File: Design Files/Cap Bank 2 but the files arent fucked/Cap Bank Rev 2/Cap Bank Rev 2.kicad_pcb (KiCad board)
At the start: 2 copper layers, 54 x 85.6 mm, 23 parts, among them J1 Conn_01x02, Q1 2N3904, Q2 2N3904, Q3 2N3904, Q4 2N3904

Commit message: updated again!!!
ship it!
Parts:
- removed C2, C4, C6, C8: C_Polarized, Library:smallcap
- added ?: , , F.Cu at (150.0, 111.5)
- added ?: , , F.Cu at (178.6, 127.5)
- added ?: , , F.Cu at (150.0, 88.5)
- added ?: , , F.Cu at (178.6, 72.5)
- added J2: Conn_01x02, Connector_AMASS:AMASS_XT30U-F_1x02_P5.0mm_Vertical, F.Cu at (131.0, 103.2)
- C1, C5: footprint Library:bigcap2pos -> Library:bigcap
- C3, C7: footprint Library:bigcap2neg -> Library:bigcap
- J1: footprint Library:xt30 -> Connector_AMASS:AMASS_XT30U-M_1x02_P5.0mm_Vertical
- moved REF** 23.0 mm to (150.0, 111.5)
- moved REF** 23.0 mm to (150.0, 88.5)
- moved J1 7.08 mm to (131.0, 96.8), turned to 180 degrees
- moved C1 5.21 mm to (137.5, 121.5)
- moved C3 5.21 mm to (162.5, 121.5)
- moved C5 5.21 mm to (162.5, 78.5)
- moved C7 5.21 mm to (137.5, 78.5)
- moved Q1 2.00 mm to (140.0, 103.0)
- moved Q2 2.00 mm to (160.0, 103.0)
- moved Q3 2.00 mm to (160.0, 97.0)
- moved Q4 2.00 mm to (140.0, 97.0)
- moved R1 2.00 mm to (136.0, 101.2)
- moved R2 2.00 mm to (144.0, 101.2)
- moved R3 2.00 mm to (156.0, 101.2)
- moved R4 2.00 mm to (164.0, 101.2)
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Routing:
- net /V_IN: track 4.40 -> 0.40 mm
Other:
- board size 54 x 85.6 mm -> 62 x 67 mm

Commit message: new bjt
who dis
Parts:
- added D1: LED, LED_THT:LED_D3.0mm_Clear, F.Cu at (128.6, 84.4)
- added R9: 1000, Resistor_THT:R_Axial_DIN0207_L6.3mm_D2.5mm_P7.62mm_Horizontal, F.Cu at (123.0, 92.0)
- Q1, Q2, Q3, Q4: value 2N3904 -> TIP31; footprint Library:2n3904 -> Library:tip31
- moved ? 57.3 mm to (121.4, 127.5)
- moved ? 57.3 mm to (121.4, 72.5)
- moved R6 11.1 mm to (165.4, 92.9), turned to 180 degrees
- moved R2 10.7 mm to (134.8, 106.7), turned to 0 degrees
- moved R8 9.96 mm to (144.1, 92.9), turned to 180 degrees
- moved R4 9.92 mm to (155.7, 106.7), turned to 0 degrees
- moved Q4 8.97 mm to (138.9, 88.1), turned to 180 degrees
- moved Q3 8.82 mm to (160.4, 88.2), turned to 180 degrees
- moved Q1 8.63 mm to (139.8, 111.6), turned to 0 degrees
- moved Q2 8.58 mm to (160.7, 111.5), turned to 0 degrees
- moved R5 4.70 mm to (167.9, 96.2), turned to 180 degrees
- moved C7 4.61 mm to (137.8, 73.9)
- moved C5 4.48 mm to (161.8, 74.1)
- moved C3 3.90 mm to (161.4, 125.2)
- moved C1 3.78 mm to (137.3, 125.3)
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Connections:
- C3 pad 1: Net-(Q1-E) -> Net-(Q2-C)
- C5 pad 1: Net-(Q2-E) -> Net-(Q3-C)
- C7 pad 1: Net-(Q3-E) -> Net-(Q4-C)
- Q1 pad 1: Net-(Q1-E) -> Net-(Q1-B)
- Q1 pad 2: Net-(Q1-B) -> /V_IN
- Q1 pad 3: /V_IN -> Net-(Q1-E)
- Q2 pad 1: Net-(Q2-E) -> Net-(Q2-B)
- Q2 pad 2: Net-(Q2-B) -> Net-(Q2-C)
- Q2 pad 3: Net-(Q1-E) -> Net-(Q2-E)
- Q3 pad 1: Net-(Q3-E) -> Net-(Q3-B)
- Q3 pad 2: Net-(Q3-B) -> Net-(Q3-C)
- Q3 pad 3: Net-(Q2-E) -> Net-(Q3-E)
- Q4 pad 1: /GND -> Net-(Q4-B)
- Q4 pad 2: Net-(Q4-B) -> Net-(Q4-C)
- Q4 pad 3: Net-(Q3-E) -> /GND
- R3 pad 2: Net-(Q1-E) -> Net-(Q2-C)
- R5 pad 2: Net-(Q2-E) -> Net-(Q3-C)
- R7 pad 2: Net-(Q3-E) -> Net-(Q4-C)
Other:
- board size 62 x 67 mm -> 57 x 75.1 mm

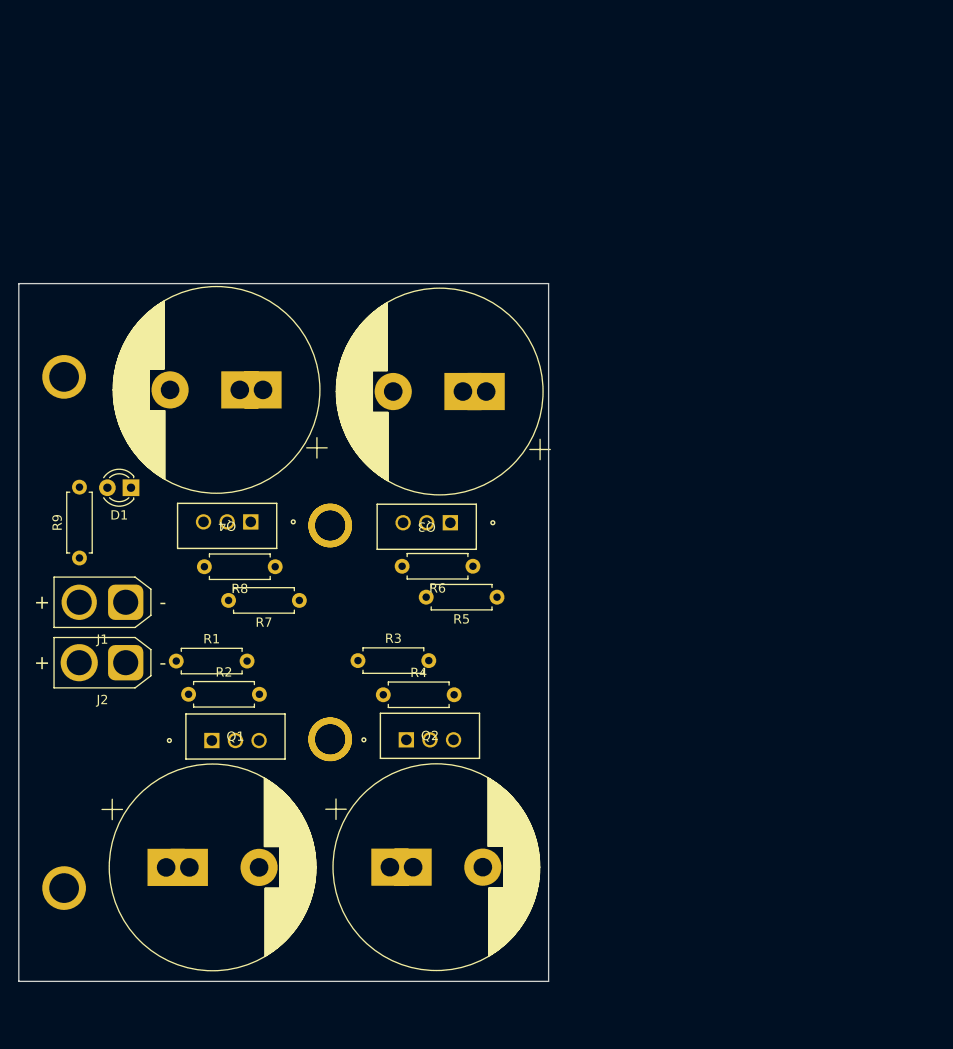
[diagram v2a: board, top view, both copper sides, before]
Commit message: NO HEATSINKS
they were too large...
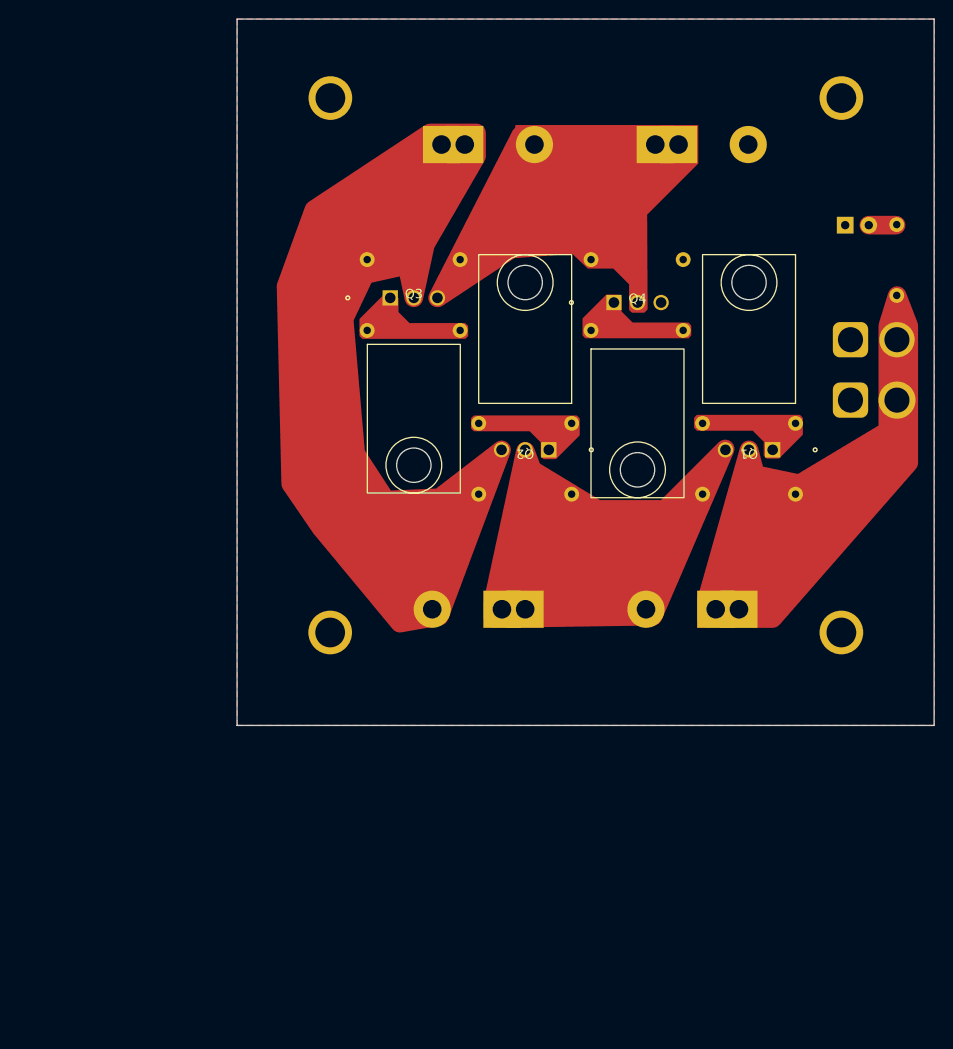
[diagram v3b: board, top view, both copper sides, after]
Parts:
- removed the ? at (150.0, 111.5)
- removed the ? at (121.4, 127.5)
- removed the ? at (150.0, 88.5)
- removed the ? at (121.4, 72.5)
- removed REF** (x2): MountingHole_3.2mm_M3, PassiveBankV1:MountingHole_3.2mm_M3
- added ?: , , F.Cu at (150.0, 42.5)
- added ?: , , F.Cu at (150.0, 100.0)
- added ?: , , F.Cu at (205.0, 42.5)
- added ?: , , F.Cu at (205.0, 100.0)
- C1, C3, C5, C7, D1, J1, J2, R1, R2, R3, R4, R5, R6, R7, R8: moved to B.Cu
- Q1, Q2, Q3, Q4: footprint Library:tip31 -> Library:tip31sideways
- R9: value 1000 -> 1740; moved to B.Cu
- moved R9 92.4 mm to (211.0, 63.7)
- moved J1 82.9 mm to (206.0, 68.5), turned to 0 degrees
- moved J2 82.9 mm to (206.0, 75.0), turned to 0 degrees
- moved D1 81.9 mm to (205.4, 56.2), turned to 0 degrees
- moved R1 71.4 mm to (200.1, 77.5), turned to -90 degrees
- moved Q1 63.5 mm to (195.1, 80.3), turned to 180 degrees
- moved R2 62.5 mm to (190.1, 77.5), turned to -90 degrees
- moved C1 58.6 mm to (189.0, 97.5), turned to 180 degrees
- moved C7 58.5 mm to (190.0, 47.5), turned to 0 degrees
- moved R8 50.7 mm to (188.0, 67.5), turned to 90 degrees
- moved Q4 50.1 mm to (183.1, 64.5), turned to 0 degrees
- moved R7 42.8 mm to (178.1, 67.5), turned to 90 degrees
- moved R3 34.4 mm to (176.0, 77.5), turned to -90 degrees
- moved Q2 32.8 mm to (171.0, 80.3), turned to 180 degrees
- moved R5 31.9 mm to (154.0, 67.5), turned to 90 degrees
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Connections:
- C3 pad 1: Net-(Q2-C) -> Net-(Q1-E)
- C5 pad 1: Net-(Q3-C) -> Net-(Q2-E)
- C7 pad 1: Net-(Q4-C) -> Net-(Q3-E)
- Q2 pad 2: Net-(Q2-C) -> Net-(Q1-E)
- Q3 pad 2: Net-(Q3-C) -> Net-(Q2-E)
- Q4 pad 2: Net-(Q4-C) -> Net-(Q3-E)
- R3 pad 2: Net-(Q2-C) -> Net-(Q1-E)
- R5 pad 2: Net-(Q3-C) -> Net-(Q2-E)
- R7 pad 2: Net-(Q4-C) -> Net-(Q3-E)
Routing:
- net Net-(D1-A): track 0.00 -> 3.03 mm
- added copper zone on F.Cu, net /GND
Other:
- board size 57 x 75.1 mm -> 75 x 76 mm
